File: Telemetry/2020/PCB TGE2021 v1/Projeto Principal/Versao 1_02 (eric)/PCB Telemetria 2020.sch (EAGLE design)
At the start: 39 parts, among them IC1 INA240A1DR, IC2 MCP3221A6T-E_OTVAO, IC3 AZ1117IH-3.3TRG1, IC4 ACS758LCB-050B-PFF-T, IC5 ADS1115IDGSR, U1 ACS712ELCTR30AT

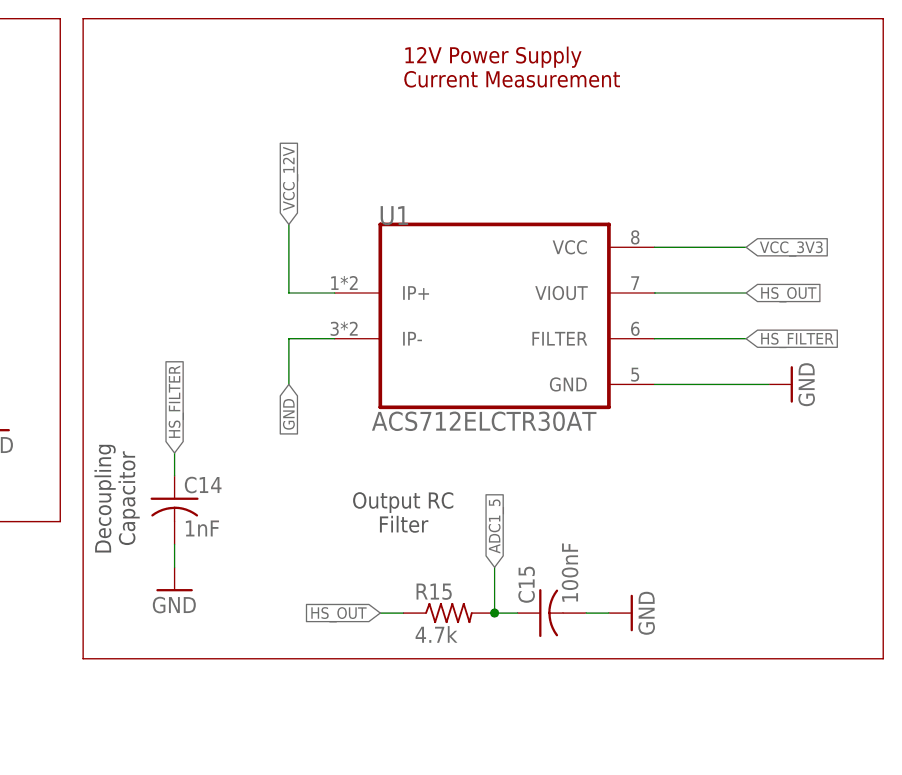
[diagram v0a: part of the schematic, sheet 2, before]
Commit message: Atualizando para o modelo correto do Sensor Hall
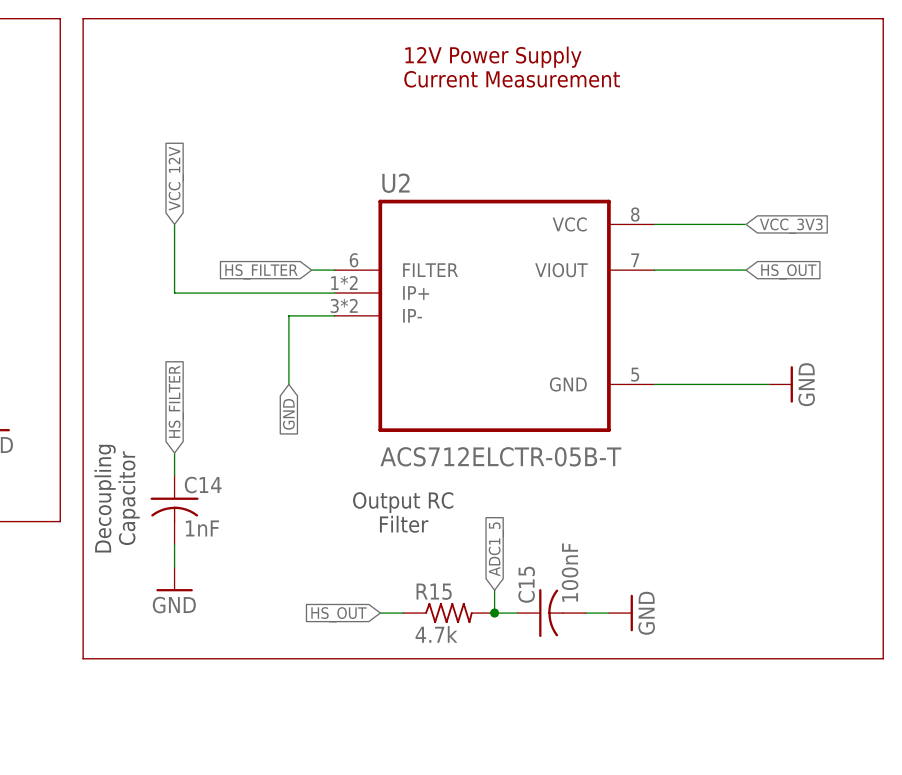
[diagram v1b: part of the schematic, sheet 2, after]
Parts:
- removed U1: ACS712ELCTR30AT, ACS712ELCTR30AT:ACS712ELCTR30AT
- added U2: ACS712ELCTR-05B-T, ACS712ELCTR-05B-T:ACS712ELCTR-05B-T
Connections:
- net GND: now also U2.GND, U2.IP-; no longer U1.GND, U1.IP-
- net HS_FILTER: now also U2.FILTER; no longer U1.FILTER
- net HS_OUT: now also U2.VIOUT; no longer U1.VIOUT
- net VCC_12V: now also U2.IP+; no longer U1.IP+
- net VCC_3V3: now also U2.VCC; no longer U1.VCC
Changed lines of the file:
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@@
 <part name="R15" library="rcl" library_urn="urn:adsk.eagle:library:334" deviceset="R-US_" device="R0805" package3d_urn="urn:adsk.eagle:package:23553/2" value="4.7k"/>
 <part name="GND17" library="supply1" library_urn="urn:adsk.eagle:library:371" deviceset="GND" device=""/>
-<part name="U1" library="ACS712ELCTR30AT" deviceset="ACS712ELCTR30AT" device=""/>
+<part name="U2" library="ACS712ELCTR-05B-T" deviceset="ACS712ELCTR-05B-T" device=""/>
 </parts>
 <sheets>
@@
 <attribute name="VALUE" x="355.6" y="149.86" size="1.778" layer="96" rot="R90"/>
 </instance>
-<instance part="U1" gate="G$1" x="337.82" y="185.42" smashed="yes">
-<attribute name="NAME" x="324.9336" y="195.5287" size="2.08621875" layer="95" ratio="10" rot="SR0"/>
-<attribute name="VALUE" x="324.1724" y="172.6631" size="2.08746875" layer="96" ratio="10" rot="SR0"/>
+<instance part="U2" gate="A" x="337.82" y="185.42" smashed="yes">
+<attribute name="NAME" x="325.12" y="199.12" size="2.0828" layer="95" ratio="10" rot="SR0"/>
+<attribute name="VALUE" x="325.12" y="168.72" size="2.0828" layer="96" ratio="10" rot="SR0"/>
 </instance>
 </instances>
@@
 <pinref part="GND15" gate="1" pin="GND"/>
 <wire x1="355.6" y1="177.8" x2="368.3" y2="177.8" width="0.1524" layer="91"/>
-<pinref part="U1" gate="G$1" pin="GND"/>
+<pinref part="U2" gate="A" pin="GND"/>
 </segment>
 <segment>
@@
 </segment>
 <segment>
-<wire x1="314.96" y1="182.88" x2="314.96" y2="177.8" width="0.1524" layer="91"/>
+<wire x1="314.96" y1="185.42" x2="314.96" y2="177.8" width="0.1524" layer="91"/>
 <label x="314.96" y="177.8" size="1.27" layer="95" rot="R270" xref="yes"/>
-<pinref part="U1" gate="G$1" pin="IP-"/>
-<wire x1="320.04" y1="182.88" x2="314.96" y2="182.88" width="0.1524" layer="91"/>
+<wire x1="320.04" y1="185.42" x2="314.96" y2="185.42" width="0.1524" layer="91"/>
+<pinref part="U2" gate="A" pin="IP-"/>
 </segment>
 </net>
@@
 </segment>
 <segment>
-<label x="365.76" y="193.04" size="1.27" layer="95" xref="yes"/>
-<wire x1="365.76" y1="193.04" x2="355.6" y2="193.04" width="0.1524" layer="91"/>
-<pinref part="U1" gate="G$1" pin="VCC"/>
+<label x="365.76" y="195.58" size="1.27" layer="95" xref="yes"/>
+<wire x1="365.76" y1="195.58" x2="355.6" y2="195.58" width="0.1524" layer="91"/>
+<pinref part="U2" gate="A" pin="VCC"/>
 </segment>
 </net>
@@
 </segment>
 <segment>
-<wire x1="314.96" y1="187.96" x2="314.96" y2="195.58" width="0.1524" layer="91"/>
-<label x="314.96" y="195.58" size="1.27" layer="95" rot="R90" xref="yes"/>
-<pinref part="U1" gate="G$1" pin="IP+"/>
-<wire x1="320.04" y1="187.96" x2="314.96" y2="187.96" width="0.1524" layer="91"/>
+<wire x1="302.26" y1="187.96" x2="302.26" y2="195.58" width="0.1524" layer="91"/>
+<label x="302.26" y="195.58" size="1.27" layer="95" rot="R90" xref="yes"/>
+<wire x1="320.04" y1="187.96" x2="302.26" y2="187.96" width="0.1524" layer="91"/>
+<pinref part="U2" gate="A" pin="IP+"/>
 </segment>
 </net>
 <net name="HS_OUT" class="0">
 <segment>
-<wire x1="355.6" y1="187.96" x2="365.76" y2="187.96" width="0.1524" layer="91"/>
-<label x="365.76" y="187.96" size="1.27" layer="95" xref="yes"/>
-<pinref part="U1" gate="G$1" pin="VIOUT"/>
+<wire x1="355.6" y1="190.5" x2="365.76" y2="190.5" width="0.1524" layer="91"/>
+<label x="365.76" y="190.5" size="1.27" layer="95" xref="yes"/>
+<pinref part="U2" gate="A" pin="VIOUT"/>
 </segment>
 <segment>
@@
 <pinref part="R15" gate="G$1" pin="2"/>
 <wire x1="340.36" y1="152.4" x2="337.82" y2="152.4" width="0.1524" layer="91"/>
-<wire x1="337.82" y1="152.4" x2="337.82" y2="157.48" width="0.1524" layer="91"/>
+<wire x1="337.82" y1="152.4" x2="337.82" y2="154.94" width="0.1524" layer="91"/>
 <junction x="337.82" y="152.4"/>
-<label x="337.82" y="157.48" size="1.27" layer="95" rot="R90" xref="yes"/>
+<label x="337.82" y="154.94" size="1.27" layer="95" rot="R90" xref="yes"/>
 </segment>
 </net>
@@
 </segment>
 <segment>
-<pinref part="U1" gate="G$1" pin="FILTER"/>
-<wire x1="355.6" y1="182.88" x2="365.76" y2="182.88" width="0.1524" layer="91"/>
-<label x="365.76" y="182.88" size="1.27" layer="95" xref="yes"/>
-</segment>
-</net>
+<wire x1="320.04" y1="190.5" x2="317.5" y2="190.5" width="0.1524" layer="91"/>
+<label x="317.5" y="190.5" size="1.27" layer="95" rot="R180" xref="yes"/>
+<pinref part="U2" gate="A" pin="FILTER"/>
+</segment>
+</net>
